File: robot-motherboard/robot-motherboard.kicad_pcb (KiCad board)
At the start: 2 copper layers, 129.3 x 78.7 mm, 67 parts, among them J1 Wing0_S, J10 Reflectance, J11 Arm_I, J12 Intake_I, J13 User.Input, J14 I2C0, J15 Extra, J16 I2C1, J17 PW_OUT, J18 Encoder1, J19 Basket_S, J2 Wing0_SW, J20 Encoder0, J3 BATT, J4 Wing1_S, J5 Wing1_SW, J6 9V, J7 Drivetrain_M, J8 Arm_M, J9 Arm_M, Q1 IRFZ44, SW1 ENC0.A/IN.SEL0, SW2 ENC0.B/IN.SEL1, SW3 ENC1.A/IN.SEL2, SW4 ENC1.B/IN.ADC, U1 MCT6, U2 LM2596_Breakout, U3 CD4051B, U4 ESP32_PICO-1, U5 BNO085

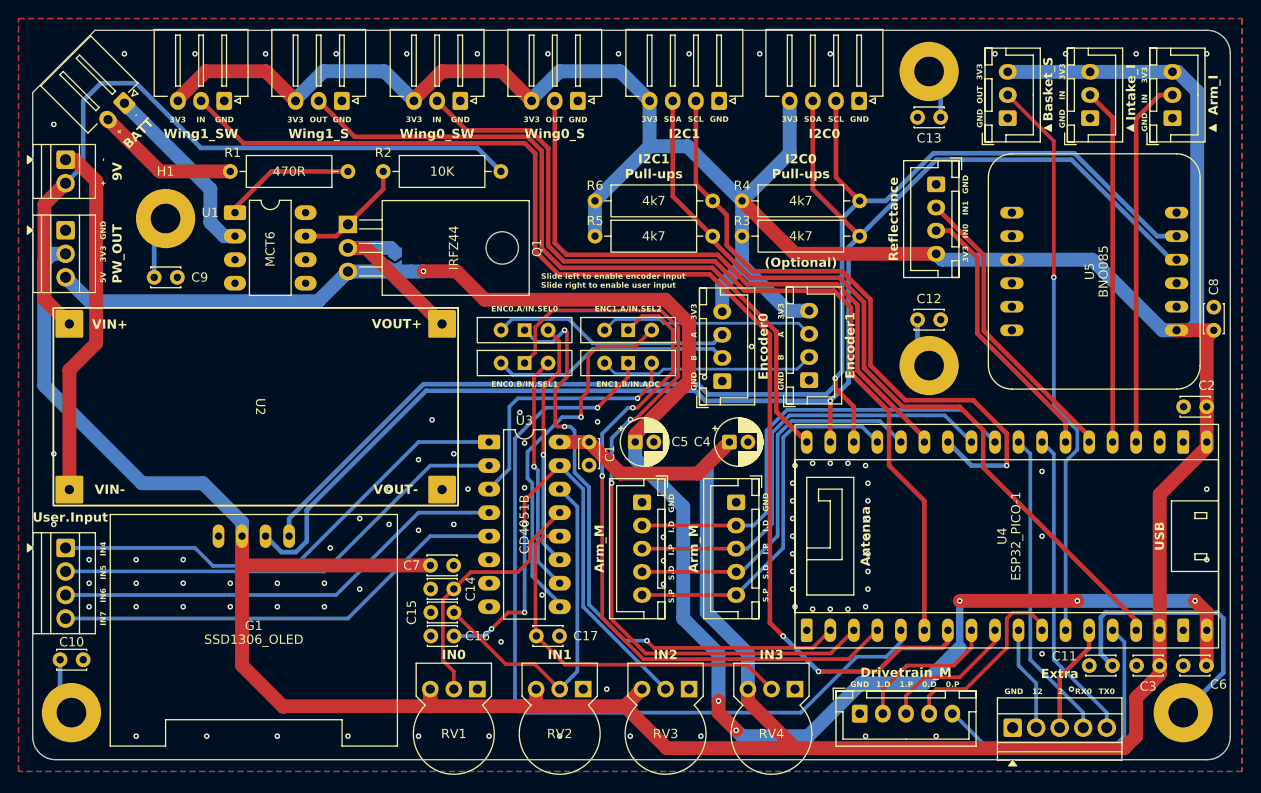
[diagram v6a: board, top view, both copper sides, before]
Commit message: Update to the right ESP32 footprint
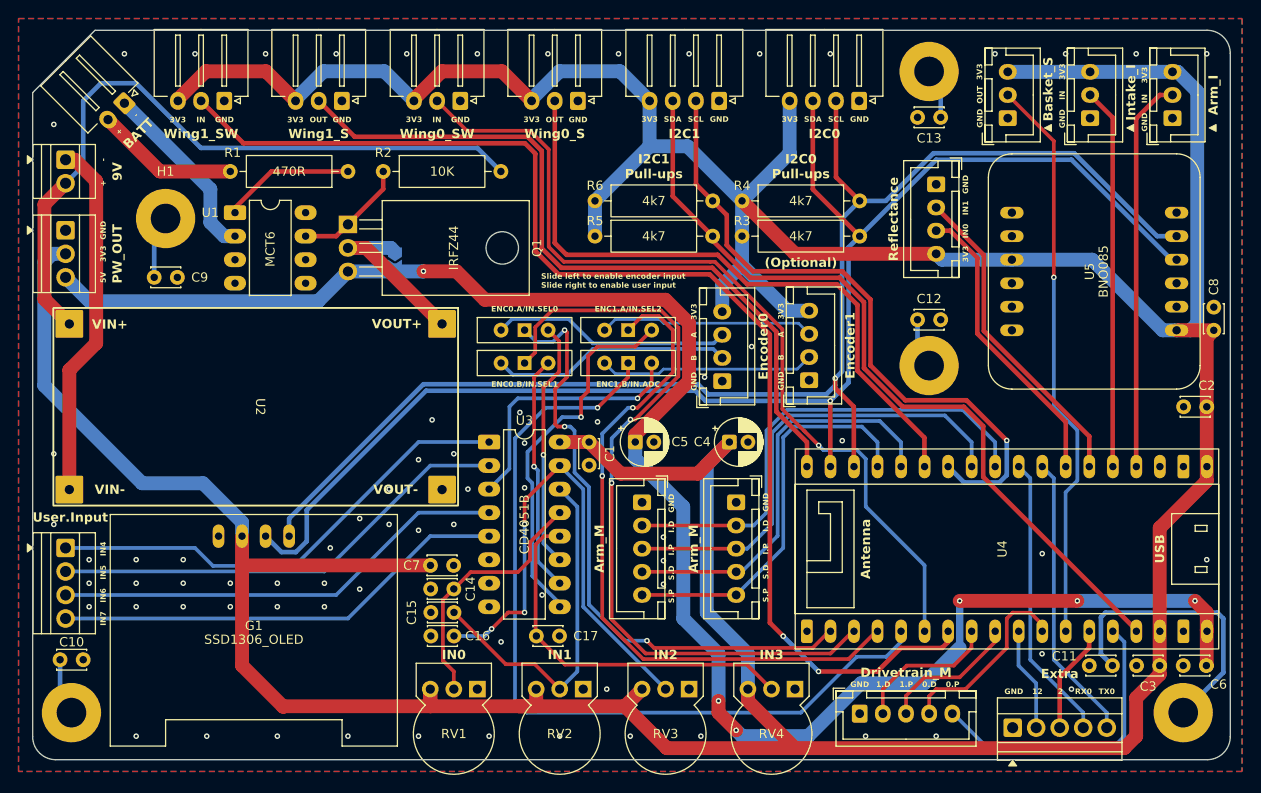
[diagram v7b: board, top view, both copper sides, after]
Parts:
- moved U4 1.38 mm to (236.2, 90.9)
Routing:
- net /WING0.LIMIT_SW_IN: track 98.2 -> 94.7 mm, vias 0 -> 1
- net /WING0.SERVO: track 68.6 -> 71.2 mm
- net /IR1.IN: track 32.2 -> 34.8 mm
- net /ARM.POSITION: track 39.9 -> 42.6 mm
- net /ARM.INTAKE_SW: track 38.5 -> 41.1 mm
- net /I2C0.SDA: track 153.7 -> 156.3 mm
- net /I2C0.SCL: track 148.3 -> 151.0 mm
- net /ARM.SHOULDER_PWM: track 40.6 -> 43.3 mm
- net /ARM.INTAKE_PWM: track 48.5 -> 51.1 mm
- net /WING1.SERVO: track 79.2 -> 81.8 mm
- net /IR0.IN: track 29.5 -> 32.1 mm
- net /ARM.SHOULDER_DIR: track 42.0 -> 44.7 mm
- net /ARM.INTAKE_DIR: track 49.9 -> 52.6 mm
- net /TX0: track 33.7 -> 31.1 mm
- net /RX0: track 33.7 -> 31.1 mm
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
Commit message: Fix production outputs
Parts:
- moved S1 2.91 mm to (249.4, 90.6)
